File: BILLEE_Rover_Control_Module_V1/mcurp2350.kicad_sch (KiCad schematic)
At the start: 54 parts, among them J1 2.54mm Header, SW2 KMR2, SW3 RESET SW, U15 W25Q128JVSIQTR, U16 SN74LVC244APWR, U17 ABM8-272-T3_C20625731, U18 RP2350A_C42411118, U19 SN74LVC244APWR, U21 TCA4307DGKR, U22 TCA4307DGKR

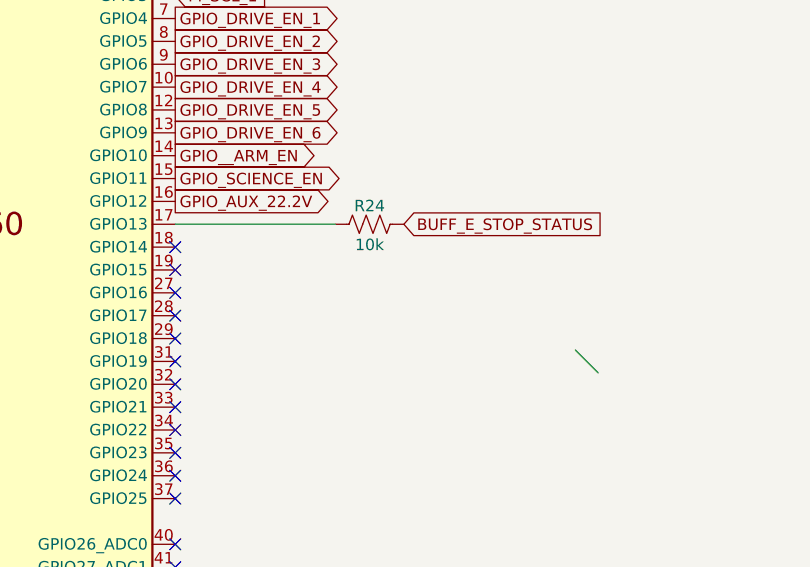
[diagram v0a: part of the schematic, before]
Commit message: Firmware Updated
INAManager, MCPManager, FPManager. Remove resistor on ESTOP BUFFER.
FPManager still needs a state machine to technically do this correctly, I dont want to rely too much on the cpp implementation
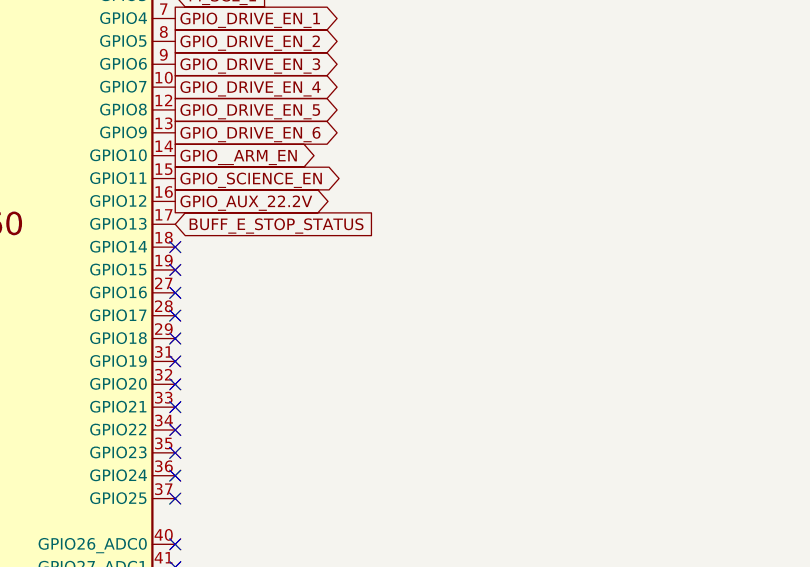
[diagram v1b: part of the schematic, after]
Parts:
- removed R24: 10k, Resistor_SMD:R_0402_1005Metric, symbol Device:R_US
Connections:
- net BUFF_E_STOP_STATUS: now also U18.17 (GPIO13)
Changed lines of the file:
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@@
 		(at 151.13 137.16)
 	)
-	(bus_entry
-		(at 195.58 130.81)
-		(size 2.54 2.54)
-		(stroke
-			(width 0)
-			(type default)
-		)
-	)
 	(wire
 		(pts
@@
 	(wire
 		(pts
-			(xy 151.13 116.84) (xy 168.91 116.84)
-		)
-		(stroke
-			(width 0)
-			(type default)
-		)
-	)
-	(wire
-		(pts
 			(xy 67.31 80.01) (xy 67.31 68.58)
 		)
@@
 	(global_label "BUFF_E_STOP_STATUS"
 		(shape input)
-		(at 176.53 116.84 0)
+		(at 151.13 116.84 0)
 		(fields_autoplaced yes)
 		(effects
@@
 		)
 		(property "Intersheetrefs" "${INTERSHEET_REFS}"
-			(at 199.8956 116.84 0)
+			(at 174.4956 116.84 0)
 			(hide yes)
 			(show_name no)
@@
 					(unit 1)
 				)
-			)
-		)
-	)
-	(symbol
-		(lib_id "Device:R_US")
-		(at 172.72 116.84 90)
-		(unit 1)
-		(body_style 1)
-		(exclude_from_sim no)
-		(in_bom yes)
-		(on_board yes)
-		(in_pos_files yes)
-		(dnp no)
-		(property "Reference" "R24"
-			(at 172.72 114.808 90)
-			(show_name no)
-			(do_not_autoplace no)
-			(effects
-				(font
-					(size 1.27 1.27)
-				)
-			)
-		)
-		(property "Value" "10k"
-			(at 172.72 119.126 90)
-			(show_name no)
-			(do_not_autoplace no)
-			(effects
-				(font
-					(size 1.27 1.27)
-				)
-			)
-		)
-		(property "Footprint" "Resistor_SMD:R_0402_1005Metric"
-			(at 172.974 115.824 90)
-			(hide yes)
-			(show_name no)
-			(do_not_autoplace no)
-			(effects
-				(font
-					(size 1.27 1.27)
-				)
-			)
-		)
-		(property "Datasheet" ""
-			(at 172.72 116.84 0)
-			(hide yes)
-			(show_name no)
-			(do_not_autoplace no)
-			(effects
-				(font
-					(size 1.27 1.27)
-				)
-			)
-		)
-		(property "Description" "Resistor, US symbol"
-			(at 172.72 116.84 0)
-			(hide yes)
-			(show_name no)
-			(do_not_autoplace no)
-			(effects
-				(font
-					(size 1.27 1.27)
-				)
-			)
-		)
-		(property "Availability" ""
-			(at 172.72 116.84 90)
-			(hide yes)
-			(show_name no)
-			(do_not_autoplace no)
-			(effects
-				(font
-					(size 1.27 1.27)
-				)
-			)
-		)
-		(property "Check_prices" ""
-			(at 172.72 116.84 90)
-			(hide yes)
-			(show_name no)
-			(do_not_autoplace no)
-			(effects
-				(font
-					(size 1.27 1.27)
-				)
-			)
-		)
-		(property "Description_1" ""
-			(at 172.72 116.84 90)
-			(hide yes)
-			(show_name no)
-			(do_not_autoplace no)
-			(effects
-				(font
-					(size 1.27 1.27)
-				)
-			)
-		)
-		(property "MANUFACTURER" ""
-			(at 172.72 116.84 90)
-			(hide yes)
-			(show_name no)
-			(do_not_autoplace no)
-			(effects
-				(font
-					(size 1.27 1.27)
-				)
-			)
-		)
-		(property "MF" ""
-			(at 172.72 116.84 90)
-			(hide yes)
-			(show_name no)
-			(do_not_autoplace no)
-			(effects
-				(font
-					(size 1.27 1.27)
-				)
-			)
-		)
-		(property "MP" ""
-			(at 172.72 116.84 90)
-			(hide yes)
-			(show_name no)
-			(do_not_autoplace no)
-			(effects
-				(font
-					(size 1.27 1.27)
-				)
-			)
-		)
-		(property "Package" ""
-			(at 172.72 116.84 90)
-			(hide yes)
-			(show_name no)
-			(do_not_autoplace no)
-			(effects
-				(font
-					(size 1.27 1.27)
-				)
-			)
-		)
-		(property "Price" ""
-			(at 172.72 116.84 90)
-			(hide yes)
-			(show_name no)
-			(do_not_autoplace no)
-			(effects
-				(font
-					(size 1.27 1.27)
-				)
-			)
-		)
-		(property "SnapEDA_Link" ""
-			(at 172.72 116.84 90)
-			(hide yes)
-			(show_name no)
-			(do_not_autoplace no)
-			(effects
-				(font
-					(size 1.27 1.27)
-				)
-			)
-		)
-		(pin "1"
-		)
-		(pin "2"
-		)
-		(instances
-			(project "BILLEE_Rover_Control_Module_V1"
-				(path "/e701dc98-f022-461d-84b5-6b2dd8d89d58/46ee40fa-f724-4b58-ad1f-c10301d1abb5"
-					(reference "R24")
-					(unit 1)
-				)

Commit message: WIP Checkpoint
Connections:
- net GPIO_AUX_22.2V: no longer U18.16 (GPIO12)
- no-connect marks 33 -> 34
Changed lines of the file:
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@@
+	)
+	(no_connect
+		(at 151.13 114.3)
 	)
 	(no_connect
@@
 			)
 		)
-	)
-	(global_label "GPIO_AUX_22.2V"
-		(shape output)
-		(at 151.13 114.3 0)
-		(fields_autoplaced yes)
-		(effects
-			(font
-				(size 1.27 1.27)
-			)
-			(justify left)
-		)
-		(property "Intersheetrefs" "${INTERSHEET_REFS}"
-			(at 169.4762 114.3 0)
-			(hide yes)
-			(show_name no)
-			(do_not_autoplace no)
-			(effects
-				(font
-					(size 1.27 1.27)
-				)
-				(justify left)
-			)
-		)

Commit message: Goodies
Updated all schematics
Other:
- company: (none) -> Bronco STAR
- title: (none) -> BILLEE_RCM
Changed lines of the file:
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@@
 	(paper "A3")
 	(title_block
-		(date "2026-07-21")
+		(title "BILLEE_RCM")
+		(date "2026-08-01")
+		(rev "A")
+		(company "Bronco STAR")
 	)
 	(rectangle

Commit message: more goodies
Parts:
- removed U19: SN74LVC244APWR, PDB_LCSC:TSSOP-20_L6.5-W4.4-P0.65-LS6.4-BL, symbol PDB_LCSC_Libs:SN74LVC244APWR
- added J2: GPIO_ADC, symbol Connector:Conn_01x04_Socket
- added J3: GPIO, symbol Connector:Conn_01x13_Socket
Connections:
- net BUFF_E_STOP_STATUS: now also U18.16 (GPIO12); no longer U18.17 (GPIO13)
- net at U18.18 (GPIO14): now also J3.2 (Pin_2)
- net at U18.19 (GPIO15): now also J3.3 (Pin_3)
- net at U18.27 (GPIO16): now also J3.4 (Pin_4)
- net at U18.28 (GPIO17): now also J3.5 (Pin_5)
- net at U18.29 (GPIO18): now also J3.6 (Pin_6)
- net at U18.31 (GPIO19): now also J3.7 (Pin_7)
- net at U18.32 (GPIO20): now also J3.8 (Pin_8)
- net at U18.33 (GPIO21): now also J3.9 (Pin_9)
- net at U18.34 (GPIO22): now also J3.10 (Pin_10)
- net at U18.35 (GPIO23): now also J3.11 (Pin_11)
- net at U18.36 (GPIO24): now also J3.12 (Pin_12)
- net at U18.37 (GPIO25): now also J3.13 (Pin_13)
- net at U18.40 (GPIO26_ADC0): now also J2.1 (Pin_1)
- net at U18.41 (GPIO27_ADC1): now also J2.2 (Pin_2)
- net at U18.42 (GPIO28_ADC2): now also J2.3 (Pin_3)
- net at U18.43 (GPIO29_ADC3): now also J2.4 (Pin_4)
- new net: J3.1 (Pin_1), U18.17 (GPIO13)
- no-connect marks 34 -> 3

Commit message: more goodies
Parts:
- removed J2: GPIO_ADC, symbol Connector:Conn_01x04_Socket
- removed J3: GPIO, symbol Connector:Conn_01x13_Socket
- added CN14: DF11-18DP-2DSA, PDB_LCSC:CONN-TH_18P-P2.00_HCTL_HC-PHD-2X9A, symbol PDB_LCSC_Libs:DF11-18DP-2DSA
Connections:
- net +3.3V_RP2350_VCC: now also CN14.11, CN14.12
- net GND: now also CN14.10; no longer USB1.1 (GND), USB1.12 (GND), USB1.13 (SHELL), USB1.14 (SHELL)
- net USB_D+: no longer USB1.6 (DP1), USB1.8 (DP2)
- net USB_D-: no longer USB1.5 (DN2), USB1.7 (DN1)
- net VBUS_USB: no longer USB1.11 (VBUS), USB1.2 (VBUS)
- net GPIO13: now reaches U18.17 (GPIO13)
- net GPIO13: now also CN14.1
- net GPIO22: now reaches U18.34 (GPIO22)
- net GPIO22: now also CN14.18
- net GPIO23: now reaches U18.35 (GPIO23)
- net GPIO23: now also CN14.17
- net GPIO24: now reaches U18.36 (GPIO24)
- net GPIO24: now also CN14.16
- net GPIO25: now reaches U18.37 (GPIO25)
- net GPIO25: now also CN14.15
- net GPIO14: now reaches U18.18 (GPIO14)
- net GPIO14: now also CN14.2
- net GPIO15: now reaches U18.19 (GPIO15)
- net GPIO15: now also CN14.3
- net GPIO16: now reaches U18.27 (GPIO16)
- net GPIO16: now also CN14.4
- net GPIO17: now reaches U18.28 (GPIO17)
- net GPIO17: now also CN14.5
- net GPIO18: now reaches U18.29 (GPIO18)
- net GPIO18: now also CN14.6
- net GPIO19: now reaches U18.31 (GPIO19)
- net GPIO19: now also CN14.7
- net GPIO20: now reaches U18.32 (GPIO20)
- net GPIO20: now also CN14.8
- net GPIO21: now reaches U18.33 (GPIO21)
- net GPIO21: now also CN14.9
- net GPIO26_ADC0: now reaches U18.40 (GPIO26_ADC0)
- net GPIO26_ADC0: now also CN14.14
- net GPIO27_ADC1: now reaches U18.41 (GPIO27_ADC1)
- net GPIO27_ADC1: now also CN14.13
- net at R9.1: no longer USB1.4 (CC1)
- net at R10.1: no longer USB1.10 (CC2)
- no-connect marks 3 -> 5
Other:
- note added: "GPIO Breakout DF11 18DP"

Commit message: Updated for schematic review by claude
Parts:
- removed USB1: TYPE-C 16PIN 2MD, PDB_LCSC:USB-C-SMD_TYPE-C-16PIN-2MD-073, symbol PDB_LCSC_Libs:TYPE-C16PIN2MD
- added USB2: TYPE-C 16PIN 2MD, PDB_LCSC:USB-C-SMD_TYPE-C-16PIN-2MD-073, symbol PDB_LCSC_Libs:TYPE-C16PIN2MD
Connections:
- net GND: now also USB2.12 (GND), USB2.14 (SHELL)
- net USB_D+: now also USB2.6 (DP1), USB2.8 (DP2)
- net USB_D-: now also USB2.5 (DN2), USB2.7 (DN1)
- net VBUS_USB: now also USB2.11 (VBUS), USB2.2 (VBUS)
- net at R9.1: now also USB2.4 (CC1)
- net at R10.1: now also USB2.10 (CC2)
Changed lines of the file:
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@@
 	)
 	(junction
+		(at 363.22 26.67)
+		(diameter 0)
+		(color 0 0 0 0)
+	)
+	(junction
 		(at 99.06 46.99)
 		(diameter 0)
@@
 	(wire
 		(pts
-			(xy 353.06 59.69) (xy 356.87 59.69)
+			(xy 353.06 59.69) (xy 354.33 59.69)
 		)
 		(stroke
@@
 	(wire
 		(pts
+			(xy 351.79 59.69) (xy 353.06 59.69)
+		)
+		(stroke
+			(width 0)
+			(type default)
+		)
+	)
+	(wire
+		(pts
 			(xy 153.67 123.19) (xy 154.94 123.19)
 		)
@@
 	(wire
 		(pts
-			(xy 349.25 59.69) (xy 353.06 59.69)
-		)
-		(stroke
-			(width 0)
-			(type default)
-		)
-	)
-	(wire
-		(pts
 			(xy 67.31 68.58) (xy 31.75 68.58)
 		)
@@
 	)
 	(symbol
+		(lib_name "TYPE-C16PIN2MD_1")
+		(lib_id "PDB_LCSC_Libs:TYPE-C16PIN2MD")
+		(at 353.06 40.64 0)
+		(unit 1)
+		(body_style 1)
+		(exclude_from_sim no)
+		(in_bom yes)
+		(on_board yes)
+		(in_pos_files yes)
+		(dnp no)
+		(fields_autoplaced yes)
+		(property "Reference" "USB2"
+			(at 353.06 21.59 0)
+			(hide yes)
+			(show_name no)
+			(do_not_autoplace no)
+			(effects
+				(font
+					(size 1.27 1.27)
+				)
+			)
+		)
+		(property "Value" "TYPE-C 16PIN 2MD"
+			(at 353.06 59.69 0)
+			(hide yes)
+			(show_name no)
+			(do_not_autoplace no)
+			(effects
+				(font
+					(size 1.27 1.27)
+				)
+			)
+		)
+		(property "Footprint" "PDB_LCSC:USB-C-SMD_TYPE-C-16PIN-2MD-073"
+			(at 353.06 62.23 0)
+			(hide yes)
+			(show_name no)
+			(do_not_autoplace no)
+			(effects
+				(font
+					(size 1.27 1.27)
+				)
+			)
+		)
+		(property "Datasheet" "https://www.lcsc.com/datasheet/C2765186.pdf"
+			(at 353.06 64.77 0)
+			(hide yes)
+			(show_name no)
+			(do_not_autoplace no)
+			(effects
+				(font
+					(size 1.27 1.27)
+				)
+			)
+		)
+		(property "Description" ""
+			(at 353.06 40.64 0)
+			(hide yes)
+			(show_name no)
+			(do_not_autoplace no)
+			(effects
+				(font
+					(size 1.27 1.27)
+				)
+			)
+		)
+		(property "Manufacturer" "SHOU HAN(首韩)"
+			(at 353.06 67.31 0)
+			(hide yes)
+			(show_name no)
+			(do_not_autoplace no)
+			(effects
+				(font
+					(size 1.27 1.27)
+				)
+			)
+		)
+		(property "MPN" "TYPE-C 16PIN 2MD(073)"
+			(at 353.06 69.85 0)
+			(hide yes)
+			(show_name no)
+			(do_not_autoplace no)
+			(effects
+				(font
+					(size 1.27 1.27)
+				)
+			)
+		)
+		(property "LCSC Part" "C2765186"
+			(at 353.06 72.39 0)
+			(hide yes)
+			(show_name no)
+			(do_not_autoplace no)
+			(effects
+				(font
+					(size 1.27 1.27)
+				)
+			)
+		)
+		(pin "2"
+		)
+		(pin "9"
+		)
+		(pin "13"
+		)
+		(pin "14"
+		)
+		(pin "4"
+		)
+		(pin "1"
+		)
+		(pin "5"
+		)
+		(pin "3"
+		)
+		(pin "6"
+		)
+		(pin "7"
+		)
+		(pin "8"
+		)
+		(pin "11"
+		)
+		(pin "10"
+		)
+		(pin "12"
+		)
+		(instances
+			(project "BILLEE_Rover_Control_Module_V1"
+				(path "/e701dc98-f022-461d-84b5-6b2dd8d89d58/46ee40fa-f724-4b58-ad1f-c10301d1abb5"
+					(reference "USB2")
+					(unit 1)
+				)
+			)
+		)
+	)
+	(symbol
 		(lib_id "Device:R_US")
 		(at 363.22 95.25 180)
@@
 					(unit 1)
 				)
-			)
-		)
-	)
-	(symbol
-		(lib_id "PDB_LCSC_Libs:TYPE-C16PIN2MD")
-		(at 353.06 40.64 0)
-		(unit 1)
-		(body_style 1)
-		(exclude_from_sim no)
-		(in_bom yes)
-		(on_board yes)
-		(in_pos_files yes)
-		(dnp no)
-		(fields_autoplaced yes)
-		(property "Reference" "USB1"
-			(at 353.06 21.59 0)
-			(hide yes)
-			(show_name no)
-			(do_not_autoplace no)
-			(effects
-				(font
-					(size 1.27 1.27)
-				)
-			)
-		)
-		(property "Value" "TYPE-C 16PIN 2MD"
-			(at 353.06 59.69 0)
-			(hide yes)
-			(show_name no)
-			(do_not_autoplace no)
-			(effects
-				(font
-					(size 1.27 1.27)
-				)
-			)
-		)
-		(property "Footprint" "PDB_LCSC:USB-C-SMD_TYPE-C-16PIN-2MD-073"
-			(at 353.06 62.23 0)
-			(hide yes)
-			(show_name no)
-			(do_not_autoplace no)
-			(effects
-				(font
-					(size 1.27 1.27)
-				)
-			)
-		)
-		(property "Datasheet" "https://www.lcsc.com/datasheet/C2765186.pdf"
-			(at 353.06 64.77 0)
-			(hide yes)
-			(show_name no)
-			(do_not_autoplace no)
-			(effects
-				(font
-					(size 1.27 1.27)
-				)
-			)
-		)
-		(property "Description" ""
-			(at 353.06 40.64 0)
-			(hide yes)
-			(show_name no)
-			(do_not_autoplace no)
-			(effects
-				(font
-					(size 1.27 1.27)
-				)
-			)
-		)
-		(property "Manufacturer" "SHOU HAN(首韩)"
-			(at 353.06 67.31 0)
-			(hide yes)
-			(show_name no)
-			(do_not_autoplace no)
-			(effects
-				(font
-					(size 1.27 1.27)
-				)
-			)
-		)
-		(property "MPN" "TYPE-C 16PIN 2MD(073)"
-			(at 353.06 69.85 0)
-			(hide yes)
-			(show_name no)
-			(do_not_autoplace no)
-			(effects
-				(font
-					(size 1.27 1.27)
-				)
-			)
-		)
-		(property "LCSC Part" "C2765186"
-			(at 353.06 72.39 0)
-			(hide yes)
-			(show_name no)
-			(do_not_autoplace no)
-			(effects
-				(font
-					(size 1.27 1.27)
-				)
-			)
-		)
-		(pin "A6"
-		)
-		(pin "A4B9"
-		)
-		(pin "A1B12"
-		)
-		(pin "B5"
-		)
-		(pin "B8"
-		)
-		(pin "13"
-		)
-		(pin "B1A12"
-		)
-		(pin "A5"
-		)
-		(pin "A7"
-		)
-		(pin "B4A9"
-		)
-		(pin "A8"
-		)
-		(pin "B6"
-		)
-		(pin "B7"
-		)
-		(pin "14"
-		)
-		(instances
-			(project "BILLEE_Rover_Control_Module_V1"
-				(path "/e701dc98-f022-461d-84b5-6b2dd8d89d58/46ee40fa-f724-4b58-ad1f-c10301d1abb5"
-					(reference "USB1")
-					(unit 1)
-				)

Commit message: Applied first round of Claude review suggestions.
Updated UVLO and OVLO guidelines.
Updated symbol pin mappings and net attributes. Preparing for layout
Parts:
- R10, R9: footprint EPS:R0402 -> Resistor_SMD:R_0402_1005Metric
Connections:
- net GND: now also USB2.1 (GND), USB2.13 (SHELL)
- net VREG_AVDD: no longer names the net of C5.1, R5.2, U18.46 (VREG_AVDD)

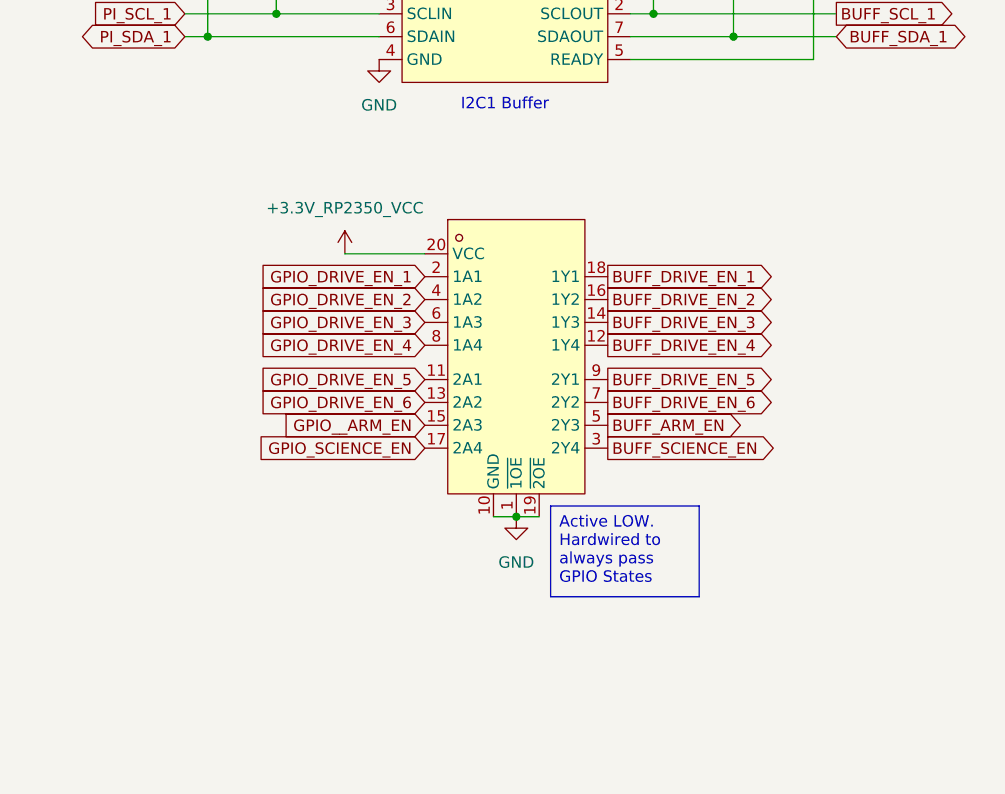
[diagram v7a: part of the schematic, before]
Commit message: Replaced GPIO buffer. Need to add reverse circuit protection. Still trying to figure out what to use
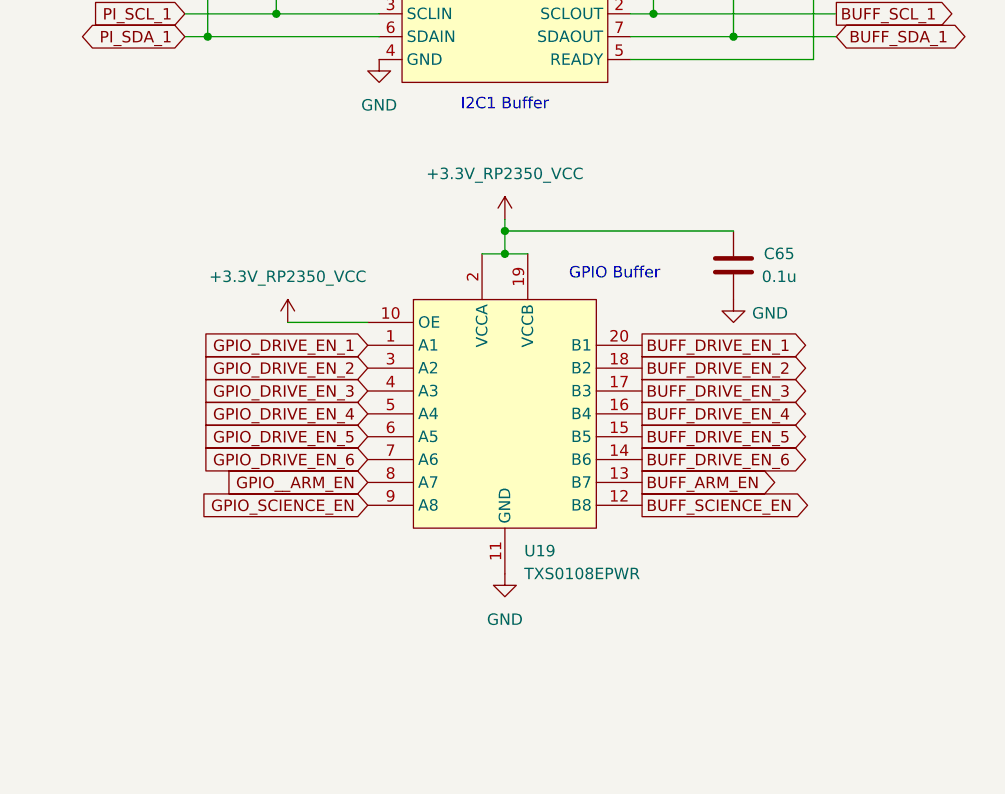
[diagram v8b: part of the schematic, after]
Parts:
- removed U16: SN74LVC244APWR, PDB_LCSC:TSSOP-20_L6.5-W4.4-P0.65-LS6.4-BL, symbol PDB_LCSC_Libs:SN74LVC244APWR
- added C65: 0.1u, Capacitor_SMD:C_0402_1005Metric, symbol Device:C
- added U19: TXS0108EPWR, PDB_LCSC:TSSOP-20_L6.5-W4.4-P0.65-LS6.4-BL, symbol PDB_LCSC_Libs:TXS0108EPWR
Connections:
- net +3.3V_RP2350_VCC: now also C65.2, U19.10 (OE), U19.19 (VCCB), U19.2 (VCCA)
- net BUFF_ARM_EN: now also U19.13 (B7)
- net BUFF_DRIVE_EN_1: now also U19.20 (B1)
- net BUFF_DRIVE_EN_2: now also U19.18 (B2)
- net BUFF_DRIVE_EN_3: now also U19.17 (B3)
- net BUFF_DRIVE_EN_4: now also U19.16 (B4)
- net BUFF_DRIVE_EN_5: now also U19.15 (B5)
- net BUFF_DRIVE_EN_6: now also U19.14 (B6)
- net BUFF_SCIENCE_EN: now also U19.12 (B8)
- net GND: now also C65.1, U19.11 (GND)
- net GPIO_DRIVE_EN_1: now also U19.1 (A1)
- net GPIO_DRIVE_EN_2: now also U19.3 (A2)
- net GPIO_DRIVE_EN_3: now also U19.4 (A3)
- net GPIO_DRIVE_EN_4: now also U19.5 (A4)
- net GPIO_DRIVE_EN_5: now also U19.6 (A5)
- net GPIO_DRIVE_EN_6: now also U19.7 (A6)
- net GPIO_SCIENCE_EN: now also U19.9 (A8)
- net GPIO__ARM_EN: now also U19.8 (A7)
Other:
- note added: "GPIO Buffer"
